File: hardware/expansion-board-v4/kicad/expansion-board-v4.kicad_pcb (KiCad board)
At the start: 6 copper layers, 100 x 62 mm, 176 parts, among them J1 PinHeader_2x20_P2.54mm_Vertic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, J2 U.FL_Hirose_U.FL-R-SMT-1_Vert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, J4 USB_C_Receptacle_HRO_TYPE-C-3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, J5 U.FL_Hirose_U.FL-R-SMT-1_Vert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, J6 U.FL_Hirose_U.FL-R-SMT-1_Vert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, J7 U.FL_Hirose_U.FL-R-SMT-1_Vert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, J8 U.FL_Hirose_U.FL-R-SMT-1_Vert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, J9 MX1.25WT-2P, Q2 SOT-23, Q3 SOT-23, Q4 SOT-23, Q5 SOT-23, SW2 SolderJumper-2_P1.3mm_Open_Pa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, U1 SOT-23-5, U10 QFN-48-1EP_7x7mm_P0.5mm_EP5.1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, U11 DFN-8-1EP_2x2mm_P0.5mm_EP0.86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, U12 SOT-363_SC-70-6, U13 AD8319_LFCSP-8-EP, U14 MSOP-8_3x3mm_P0.65mm, U15 SOT-23-6, U16 SOT-363_SC-70-6, U17 SOT-363_SC-70-6, U18 SOIC-10_3.9x4.9mm_P1mm, U19 QFN-24-1EP_4x4mm_P0.5mm_EP2.6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, U2 SOT-23-5, U20 TSOT-23-6, U3 SOT-23-5, U4 BNO085_LGA-28, U5 BMP388_LGA-10, U6 LGA-16_3x3mm_P0.5mm, U7 ATGM336H_LCC-18, U8 QFN-56-1EP_7x7mm_P0.4mm_EP3.2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, U9 SOIC-8_5.3x5.3mm_P1.27mm, Y1 Crystal_SMD_3225-4Pin_3.2x2.5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, Y2 Crystal_SMD_3225-4Pin_3.2x2.5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, Y3 Crystal_SMD_3215-2Pin_3.2x1.5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

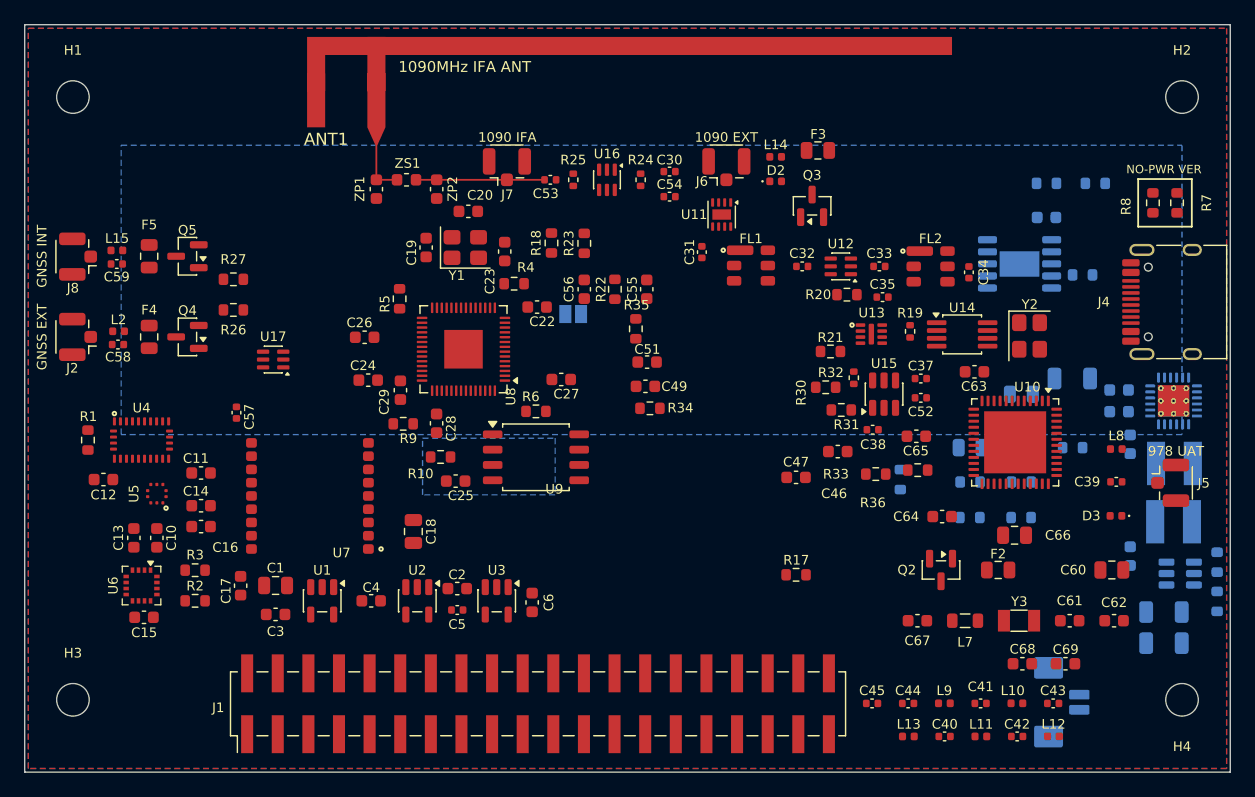
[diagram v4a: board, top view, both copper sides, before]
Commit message: fix(v4): 固化板级丝印文字 + 加护栏，修「丝印一直回归」的根因
## 根因

固化一块板需要三份数据，我一直只做了一份半：
    PLACEMENT.py  元件/位号   ← export_placement.py    ✅ 每轮都跑
    ROUTES.json   走线        ← export_routes.py
    SILK.json     板级文字     ← silk_texts.py export   ❌ 从来没跑过

板级文字（品牌、接口标注、天线标注、版本号、BATT 极性）不属于任何封装，
PLACEMENT.SILK_REF 那张表只存位号，存不下它们。

结果 SILK.json 停在 V3.5 时代：板上 16 条它只有 4 条，其中三条坐标差
14.50 / 21.45 / 29.31mm，还留着一条板上早已删除的 'V3.5   2026-08'。

平时看不出来——gen_silk.py 的优先级是「板上已有同内容文字就一个字不动」。
但只要 gen_pcb.py 从零重建一次（板级文字被清空），4 条按旧坐标贴回、
另外 12 条重新自动排版，手调位置全丢。这就是「丝印一直回归」的机制。

## 修

1. 跑 silk_texts.py export，SILK.json 4 → 16 条，三条陈旧坐标修正，幽灵条目删除
2. export_placement.py 末尾加新鲜度护栏：板级文字与 SILK.json 逐条比对
   （缺失/幽灵/坐标差 >0.05mm），不一致直接 AssertionError 并给出修复命令。
   正负向都测过：同步时打印「SILK.json 同步 ✓（16 条）」，
   换回旧 SILK.json 立刻退出码 1 并列出全部 12 条差异。

## 本轮布局（用户手工，48 件）

DRC 14 → 7（silk_overlap 6→1、silk_over_copper 2→0），未连接 298、parity 0。
3V3_DIG 去耦收到 2.80~4.84mm、RP_1V1 3.05/4.64mm、晶振组 3.44~7.81mm。
1090 链 87.12mm（东侧未动）。IFA 走廊幂等 + 5 项测试通过。

⚠️ 遗留：U8 扇出通道容量不足——下边需 8 根只可走 5 根、左边需 10 只可走 5、
右边需 10 只可走 7。去耦贴得太紧把引脚出线口堵了（2026-08-23 同类问题重现）。
fix_decap_fanout.py 给出方案：C28/C24/C23 各退 1.2~2.0mm 即可全部转正。
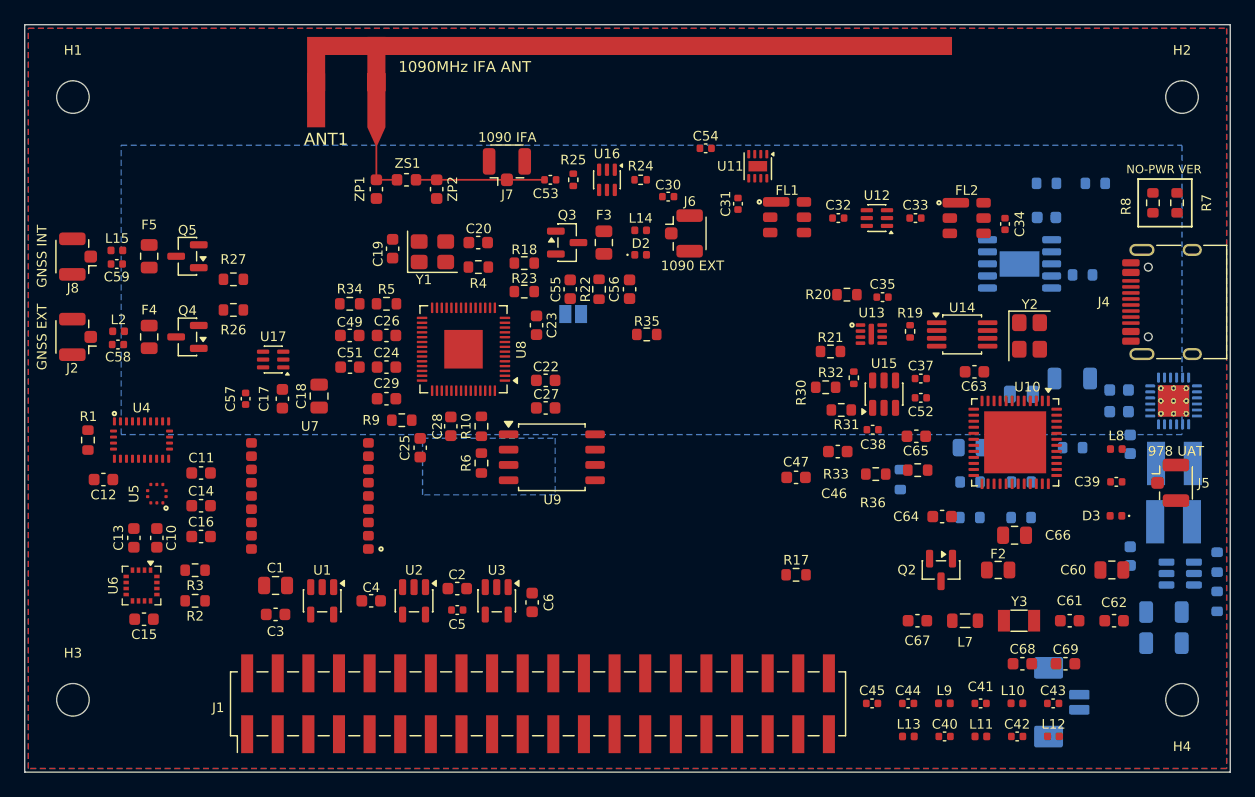
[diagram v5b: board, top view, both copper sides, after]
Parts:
- moved R34 26.4 mm to (77.0, 73.2)
- moved C49 24.9 mm to (77.0, 75.8), turned to 180 degrees
- moved C51 24.7 mm to (77.0, 78.4), turned to 180 degrees
- moved Q3 20.5 mm to (95.0, 68.1), turned to 0 degrees
- moved F3 19.3 mm to (98.0, 68.1), turned to 90 degrees
- moved C17 15.9 mm to (71.4, 81.0), turned to 90 degrees
- moved C18 13.7 mm to (74.4, 80.8), turned to 90 degrees
- moved D2 12.8 mm to (101.1, 69.1)
- moved L14 12.8 mm to (101.1, 67.1)
- moved J6 6.70 mm to (105.2, 67.3), turned to 0 degrees
- moved C23 6.66 mm to (92.5, 74.9), turned to 90 degrees
- moved R23 6.38 mm to (91.4, 72.1), turned to 0 degrees
- moved C55 6.35 mm to (95.2, 71.9)
- moved R6 6.23 mm to (87.9, 86.4), turned to 90 degrees
- moved C22 6.12 mm to (93.2, 79.5)
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
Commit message: change(v4): 检波器定为 AD8313，删除 AD8319(U13) 与 R20
## 决策依据

2026-08-01 选 AD8319 纯粹是采购逼的：当时 AD8313 立创 ¥71.37 且现货仅 5，
AD8319 ¥21.9 库存 6441。技术上 AD8319 是更差的那个：
    动态范围    AD8313 70dB   vs  AD8319 ~40dB
    预估灵敏度  ≈-105dBm      vs  -95~-100dBm
ADSBee 原设计用的也是 AD8313，所以当时留了双封装位准备投板 A/B。

现在用户在淘宝实际买到 AD8313 ¥4.8、AD8319 反而 ¥6.8，价格依据整个反转，
A/B 对比失去意义，直接定 AD8313。

顺带解决两个问题：
- U13↔U14 共享 DET_IN/DET_INLO 相隔 8.50mm，不贴的那颗是残桩，1090MHz 上影响匹配
- AD8319 是 LFCSP-8 带裸焊盘（ASSEMBLY 标 ★★★ 只能热风）；AD8313 是 MSOP-8 烙铁可焊

⚠️ 采购风险仍在：询价记录里淘宝 AD8313 低云价 1.5~5.5 被判「全是仿标」，
¥4.8 正落在该区间。上电必须验 VOUT 斜率是否为 ADI 手册的 ~18mV/dB。

## 改动

原理图源 sheet_rf1090.py：删 U13、删 R20（DET_TADJ 是 AD8319 独有的温补脚），
U14 值 "AD8313ARMZ(备,二选一)" → "AD8313ARMZ"，R21 "0R DNP(选8313时贴)" → "0R"（必贴，
AD8313_VOUT→RF_DET_OUT 现在是唯一通路）。重生成 rf1090.kicad_sch（48 符号）。

PCB：删 U13/R20 两个封装，176 → 174 件。重生成 build/netlist.xml（170 元件）。

生成脚本连带更新 7 个：gen_checklist / gen_assembly / gen_bom / gen_bom_smt /
gen_bom_xlsx / fanout_channel / ep_targets——U14 从「默认不贴」改为必贴。
gen_checklist.py 的计数断言原来把 U14 同时算进「要贴」和「不贴」，分类规则一改
就重复计数顶穿断言，一并修正。

## 验收

parity 0（原理图与 PCB 同步）、DRC 8 条 0 error、未连接 298 → 292、
IFA 走廊 5 项测试通过。C34→检波器 13.77 → 7.32mm。

遗留（均为用户手工布局，非本次引入）：
- FL1 ↔ C31 courtyard 重叠（用户在 78abd2a 后挪 C31 3.3mm 造成）
- C35 → U14 10.20mm、R21 → U14 15.40mm，需跟着 U14 重排
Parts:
- removed R20: R_0603_1608Metric, R_0603_1608Metric
- removed U13: AD8319_LFCSP-8-EP, AD8319_LFCSP-8-EP
- moved R17 27.8 mm to (93.2, 77.2), turned to 180 degrees
- moved R33 10.8 mm to (110.0, 85.1)
- moved R36 10.7 mm to (113.5, 85.1)
- moved R31 9.62 mm to (111.8, 74.4)
- moved R32 9.44 mm to (108.0, 75.9)
- moved C62 9.05 mm to (131.3, 99.6)
- moved C47 8.64 mm to (106.9, 82.5)
- moved R30 8.54 mm to (110.2, 79.0)
- moved C67 7.29 mm to (123.2, 92.2)
- moved C52 7.01 mm to (117.6, 79.0)
- moved C46 6.95 mm to (111.0, 82.8)
- moved U15 6.83 mm to (114.8, 78.5)
- moved C65 6.77 mm to (126.5, 90.4)
- moved C37 6.76 mm to (118.1, 76.7)
- moved R9 6.62 mm to (87.9, 83.3), turned to -90 degrees
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
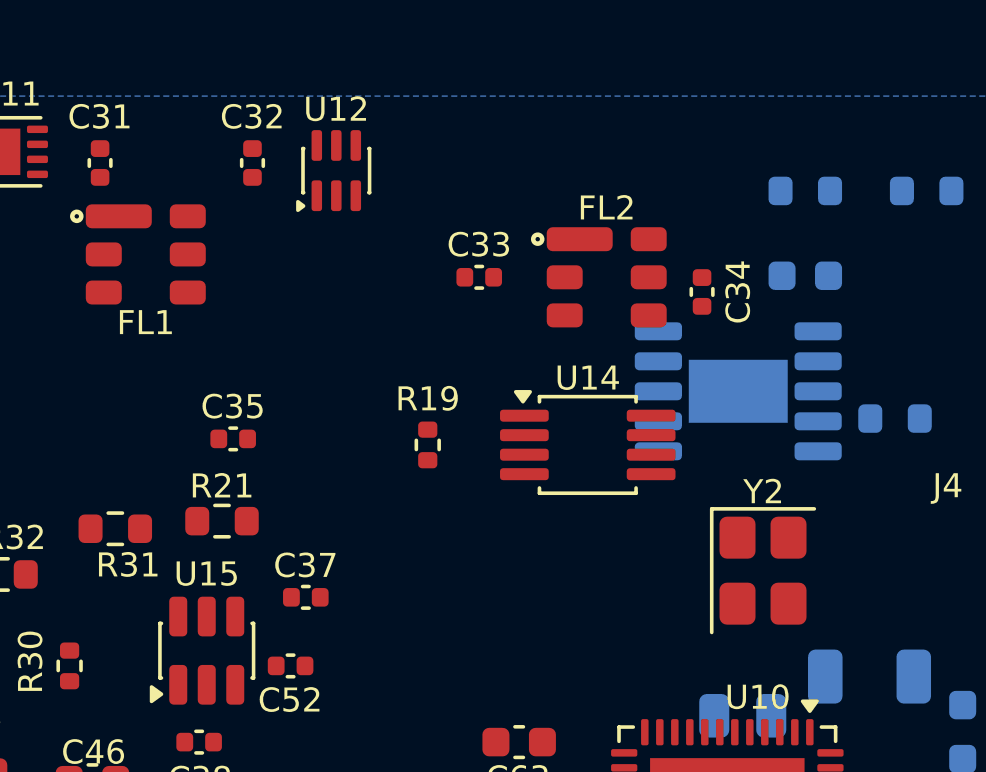
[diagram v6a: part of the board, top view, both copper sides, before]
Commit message: fix(v4): U14 转 180° 迎向 C34，R19/C35/R21 归位
U14 装反了：MSOP-8 的输入脚 DET_IN/DET_INLO 在西侧(x=125.4)，而射频源 C34
在东边(x=131.3)；输出 AD8313_VOUT 在东侧，而下游 slicer 在西边。两头都要
绕过芯片本体。转 180° 后输入迎东、输出朝西，与信号流向一致。

配套件跟到各自引脚：
  C34 ↔ U14.DET_IN        7.32 → 5.23mm   射频输入
  R19 ↔ U14 差分端接       3.23 → 2.00mm
  C35 ↔ U14.DET_INLO     10.20 → 2.80mm
  R21 ↔ U14.AD8313_VOUT  15.40 → 2.50mm

R21 是 0R 串联跳线，它在 AD8313_VOUT→RF_DET_OUT 这条线上的位置不影响电气
（总长由 U14 和 slicer 的位置决定），贴 U14 只是让残桩更短、走线更整。

DRC 9 条 0 error、未连接 292、parity 0。余下 courtyards_overlap 仍是
FL1↔C31（用户在 78abd2a 后挪 C31 造成，非本次引入）；两条 silk_overlap
是 U14/C46 位号压自身轮廓，IC 常规做法。
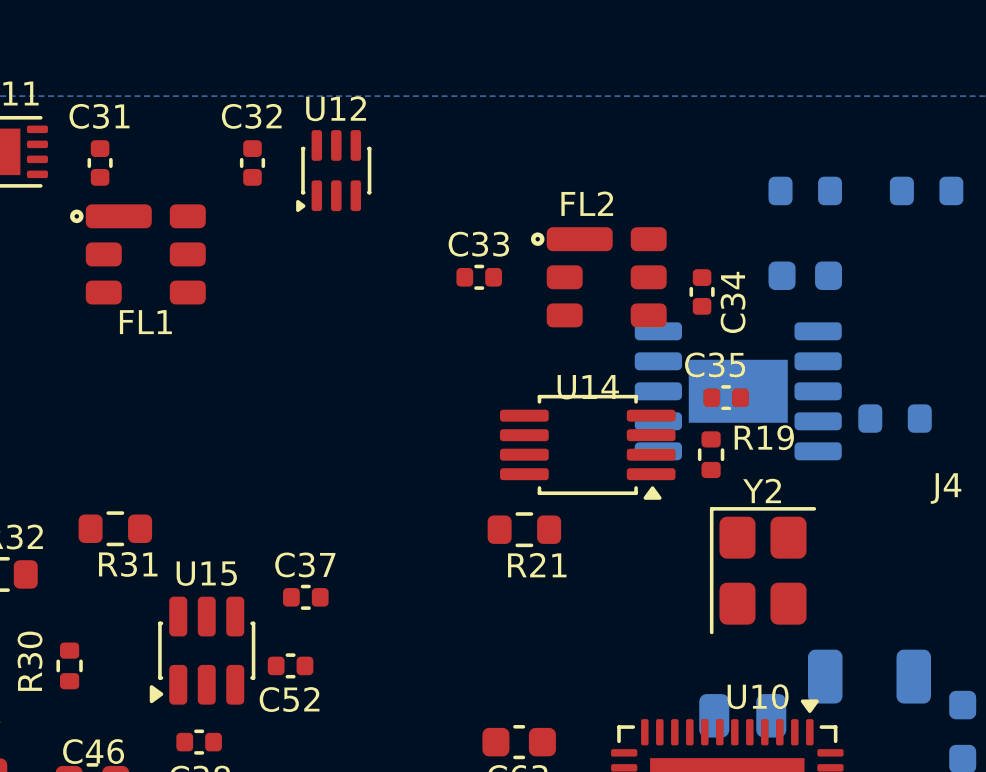
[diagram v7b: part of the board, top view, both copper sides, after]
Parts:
- moved C35 16.5 mm to (132.1, 70.1)
- moved R21 10.1 mm to (125.4, 74.5)
- moved R19 9.45 mm to (131.6, 72.0)
- turned U14 to 180 degrees
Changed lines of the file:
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@@
 	(footprint "R_0603_1608Metric"
 		(layer "F.Cu")
-		(at 115.316 74.168)
+		(at 125.395 74.453)
 		(descr "Resistor SMD 0603 (1608 Metric), square (rectangular) end terminal, IPC-7351 nominal, (Body size source: IPC-SM-782 page 72, https://www.pcb-3d.com/wordpress/wp-content/uploads/ipc-sm-782a_amendment_1_and_2.pdf)")
 		(tags "resistor")
 		(property "Reference" "R21"
-			(at 0 -1.16 0)
+			(at 0.427 1.219 0)
 			(layer "F.SilkS")
 			(effects
@@
 		(descr "TST TA0970A 1090MHz SAW 3.8x3.8, land per Rev3.0 secF (B=IN E=OUT, A long GND 2.2)")
 		(property "Reference" "FL2"
-			(at 0 -2.298 0)
+			(at -0.647 -2.415 0)
 			(layer "F.SilkS")
 			(effects
 				(font
 					(size 0.8 0.8)
-					(thickness 0.15)
+					(thickness 0.136)
 				)
 			)
@@
 	(footprint "C_0402_1005Metric"
 		(layer "F.Cu")
-		(at 115.689 71.427)
+		(at 132.12 70.053)
 		(descr "Capacitor SMD 0402 (1005 Metric), square (rectangular) end terminal, IPC-7351 nominal, (Body size source: IPC-SM-782 page 76, https://www.pcb-3d.com/wordpress/wp-content/uploads/ipc-sm-782a_amendment_1_and_2.pdf)")
 		(tags "capacitor")
 		(property "Reference" "C35"
-			(at -0.003 -1.063 180)
+			(at -0.349001 -1.063 180)
 			(layer "F.SilkS")
 			(effects
@@
 	(footprint "R_0402_1005Metric"
 		(layer "F.Cu")
-		(at 122.174 71.628 -90)
+		(at 131.62 71.953 -90)
 		(descr "Resistor SMD 0402 (1005 Metric), square (rectangular) end terminal, IPC-7351 nominal, (Body size source: IPC-SM-782 page 72, https://www.pcb-3d.com/wordpress/wp-content/uploads/ipc-sm-782a_amendment_1_and_2.pdf)")
 		(tags "resistor")
 		(property "Reference" "R19"
-			(at -1.524 0 180)
+			(at -0.537 -1.757999 180)
 			(layer "F.SilkS")
 			(effects
@@
 	(footprint "MSOP-8_3x3mm_P0.65mm"
 		(layer "F.Cu")
-		(at 127.508 71.628)
+		(at 127.508 71.628 180)
 		(descr "MSOP, 8 Pin (https://www.jedec.org/system/files/docs/mo-187F.pdf variant AA)")
 		(tags "MSOP SO")
 		(property "Reference" "U14"
-			(at 0 -2.217 0)
+			(at 0 1.9 180)
 			(layer "F.SilkS")
 			(effects
@@
 		)
 		(property "Value" "MSOP-8_3x3mm_P0.65mm"
-			(at 0 2.45 0)
+			(at 0 2.45 180)
 			(layer "F.Fab")
 			(effects
@@
 		)
 		(property "Datasheet" ""
-			(at 0 0 0)
+			(at 0 0 180)
 			(layer "F.Fab")
 			(hide yes)
@@
 		)
 		(property "Description" ""
-			(at 0 0 0)
+			(at 0 0 180)
 			(layer "F.Fab")
 			(hide yes)
@@
 		)
 		(property "KiLib_Generator" "package/gullwing"
-			(at 0 0 0)
+			(at 0 0 180)
 			(layer "F.SilkS")
 			(hide yes)
@@
 		(duplicate_pad_numbers_are_jumpers no)
 		(fp_line
-			(start -1.61 -1.61)
-			(end 1.61 -1.61)
+			(start 1.61 1.61)
+			(end -1.61 1.61)
 			(stroke
 				(width 0.12)
@@
 		)
 		(fp_line
-			(start -1.61 -1.435)
-			(end -1.61 -1.61)
+			(start 1.61 1.435)
+			(end 1.61 1.61)
 			(stroke
 				(width 0.12)
@@
 		)
 		(fp_line
-			(start -1.61 1.61)
-			(end -1.61 1.435)
+			(start 1.61 -1.61)
+			(end 1.61 -1.435)
 			(stroke
 				(width 0.12)
@@
 		)
 		(fp_line
-			(start 1.61 -1.61)
-			(end 1.61 -1.435)
+			(start -1.61 1.61)
+			(end -1.61 1.435)
 			(stroke
 				(width 0.12)
@@
 		)
 		(fp_line
-			(start 1.61 1.435)
-			(end 1.61 1.61)
+			(start -1.61 -1.435)
+			(end -1.61 -1.61)
 			(stroke
 				(width 0.12)
@@
 		)
 		(fp_line
-			(start 1.61 1.61)
-			(end -1.61 1.61)
+			(start -1.61 -1.61)
+			(end 1.61 -1.61)
 			(stroke
 				(width 0.12)
@@
 		)
 		(fp_line
-			(start -3.18 -1.43)
-			(end -1.75 -1.43)
+			(start 3.18 1.43)
+			(end 1.75 1.43)
 			(stroke
 				(width 0.05)
@@
 		)
 		(fp_line
-			(start -3.18 1.43)
-			(end -3.18 -1.43)
+			(start 3.18 -1.43)
+			(end 3.18 1.43)
 			(stroke
 				(width 0.05)
@@
 		)
 		(fp_line
-			(start -1.75 -1.75)
-			(end 1.75 -1.75)
+			(start 1.75 1.75)
+			(end -1.75 1.75)
 			(stroke
 				(width 0.05)
@@
 		)
 		(fp_line
-			(start -1.75 -1.43)
-			(end -1.75 -1.75)
+			(start 1.75 1.43)
+			(end 1.75 1.75)
 			(stroke
 				(width 0.05)
@@
 		)
 		(fp_line
-			(start -1.75 1.43)
-			(end -3.18 1.43)
+			(start 1.75 -1.43)
+			(end 3.18 -1.43)
 			(stroke
 				(width 0.05)
@@
 		)
 		(fp_line
-			(start -1.75 1.75)
-			(end -1.75 1.43)
+			(start 1.75 -1.75)
+			(end 1.75 -1.43)
 			(stroke
 				(width 0.05)
@@
 		)
 		(fp_line
-			(start 1.75 -1.75)
-			(end 1.75 -1.43)
+			(start -1.75 1.75)
+			(end -1.75 1.43)
 			(stroke
 				(width 0.05)
@@
 		)
 		(fp_line
-			(start 1.75 -1.43)
-			(end 3.18 -1.43)
+			(start -1.75 1.43)
+			(end -3.18 1.43)
 			(stroke
 				(width 0.05)
@@
 		)
 		(fp_line
-			(start 1.75 1.43)
-			(end 1.75 1.75)
+			(start -1.75 -1.43)
+			(end -1.75 -1.75)
 			(stroke
 				(width 0.05)
@@
 		)
 		(fp_line
-			(start 1.75 1.75)
-			(end -1.75 1.75)
+			(start -1.75 -1.75)
+			(end 1.75 -1.75)
 			(stroke
 				(width 0.05)
@@
 		)
 		(fp_line
-			(start 3.18 -1.43)
-			(end 3.18 1.43)
+			(start -3.18 1.43)
+			(end -3.18 -1.43)
 			(stroke
 				(width 0.05)
@@
 		)
 		(fp_line
-			(start 3.18 1.43)
-			(end 1.75 1.43)
+			(start -3.18 -1.43)
+			(end -1.75 -1.43)
 			(stroke
 				(width 0.05)
@@
 		)
 		(fp_text user "${REFERENCE}"
-			(at 0 0 0)
+			(at 0 0 180)
 			(layer "F.Fab")
 			(effects
@@
 		)
 		(pad "1" smd roundrect
-			(at -2.1125 -0.975)
+			(at -2.1125 -0.975 180)
 			(size 1.625 0.4)
 			(layers "F.Cu" "F.Mask" "F.Paste")
@@
 		)
 		(pad "2" smd roundrect
-			(at -2.1125 -0.325)
+			(at -2.1125 -0.325 180)
 			(size 1.625 0.4)
 			(layers "F.Cu" "F.Mask" "F.Paste")
@@
 		)
 		(pad "3" smd roundrect
-			(at -2.1125 0.325)
+			(at -2.1125 0.325 180)
 			(size 1.625 0.4)
 			(layers "F.Cu" "F.Mask" "F.Paste")
@@
 		)
 		(pad "4" smd roundrect
-			(at -2.1125 0.975)
+			(at -2.1125 0.975 180)
 			(size 1.625 0.4)
 			(layers "F.Cu" "F.Mask" "F.Paste")
@@
 		)
 		(pad "5" smd roundrect
-			(at 2.1125 0.975)
+			(at 2.1125 0.975 180)
 			(size 1.625 0.4)
 			(layers "F.Cu" "F.Mask" "F.Paste")
@@
 		)
 		(pad "6" smd roundrect
-			(at 2.1125 0.325)
+			(at 2.1125 0.325 180)
 			(size 1.625 0.4)
 			(layers "F.Cu" "F.Mask" "F.Paste")
@@
 		)
 		(pad "7" smd roundrect
-			(at 2.1125 -0.325)
+			(at 2.1125 -0.325 180)
 			(size 1.625 0.4)
 			(layers "F.Cu" "F.Mask" "F.Paste")
@@
 		)
 		(pad "8" smd roundrect
-			(at 2.1125 -0.975)
+			(at 2.1125 -0.975 180)
 			(size 1.625 0.4)
 			(layers "F.Cu" "F.Mask" "F.Paste")
@@
 		(tags "capacitor")
 		(property "Reference" "C34"
-			(at -0.000125 -1.216759 90)
+			(at 0.349875 -1.062759 90)
 			(layer "F.SilkS")
 			(effects
 				(font
 					(size 0.8 0.8)
-					(thickness 0.15)
+					(thickness 0.136)
 				)
 			)
